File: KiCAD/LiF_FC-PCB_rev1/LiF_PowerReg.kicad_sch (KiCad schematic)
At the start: 32 parts, among them J1 VCH1_{EN}, J2 VCH2_{EN}, J27 R5V0_{EN}, J28 A3V3_{EN}, J29 R3V3_{EN}, J30 REG_{EN}, U10 TLV75533PDBV, U11 TLV75533PDBV, U9 LMR14050

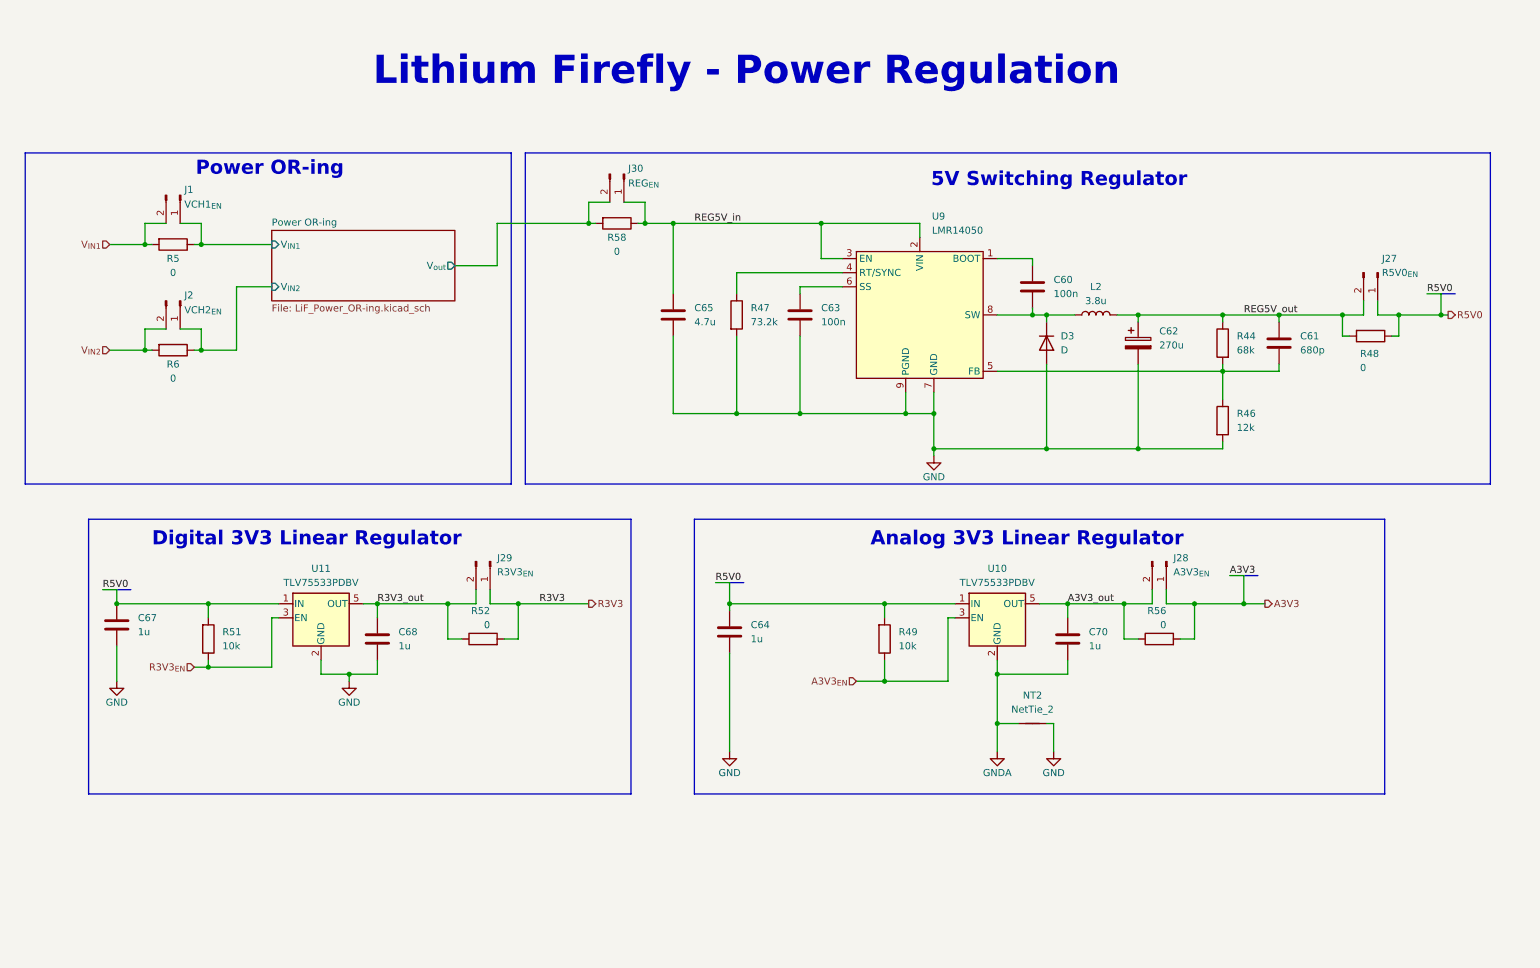
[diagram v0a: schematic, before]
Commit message: changed 5V regulator to support 5V in up to 20V in
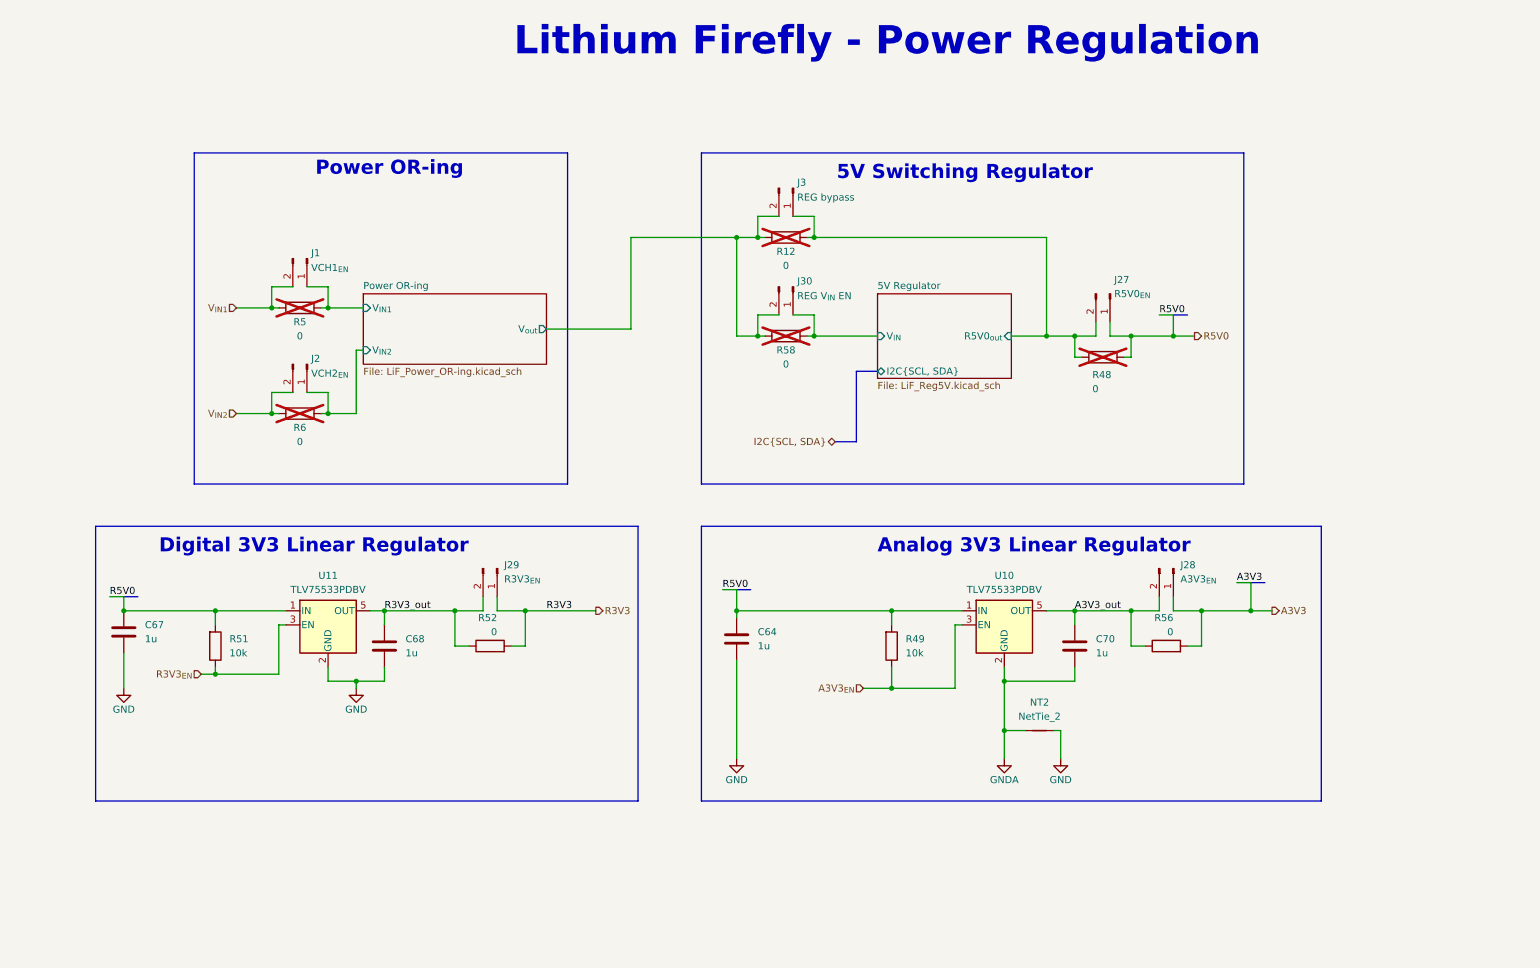
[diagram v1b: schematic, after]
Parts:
- removed C60, C63: 100n, Capacitor_SMD:C_0805_2012Metric, symbol Device:C
- removed C61: 680p, Capacitor_SMD:C_0805_2012Metric, symbol Device:C
- removed C62: 270u, Capacitor_SMD:CP_Elec_6.3x9.9, symbol Device:C_Polarized
- removed C65: 4.7u, Capacitor_SMD:C_0805_2012Metric, symbol Device:C
- removed D3: D, Diode_SMD:D_PowerDI-5, symbol Device:D
- removed L2: 3.8u, MatsLibrary:IND_BOURNS_SRU1038, symbol Device:L
- removed R44: 68k, Resistor_SMD:R_0805_2012Metric, symbol Device:R
- removed R46: 12k, Resistor_SMD:R_0805_2012Metric, symbol Device:R
- removed R47: 73.2k, Resistor_SMD:R_0805_2012Metric, symbol Device:R
- removed U9: LMR14050, Package_SO:Texas_R-PDSO-G8_EP2.95x4.9mm_Mask2.4x3.1mm, symbol MatsKiLibrary:LMR14050SDDAR
- added J3: REG bypass, Connector_PinHeader_1.27mm:PinHeader_1x02_P1.27mm_Vertical, symbol Connector:Conn_01x02_Pin
- added R12: 0, Resistor_SMD:R_0805_2012Metric, symbol Device:R
- J30: value REG_{EN} -> REG V_{IN} EN
- R48, R5, R58, R6: now not fitted
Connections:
- net Power OR-ing/V_{out}: now also J3.2 (Pin_2), R12.2
- net REG5V_in renamed 5V Regulator/V_{IN}
- net REG5V_out renamed 5V Regulator/R5V0_{out}
- net 5V Regulator/R5V0_{out}: now also J3.1 (Pin_1), R12.1
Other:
- added sheet 5V Regulator (LiF_Reg5V.kicad_sch)
- moved on the sheet: C64, C67, C68, C70, J1, J2, J27, J28, J29, J30, NT2, R49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

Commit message: reverted 5V reg, reworked power distribution logic, swapped power OR-ing ICs
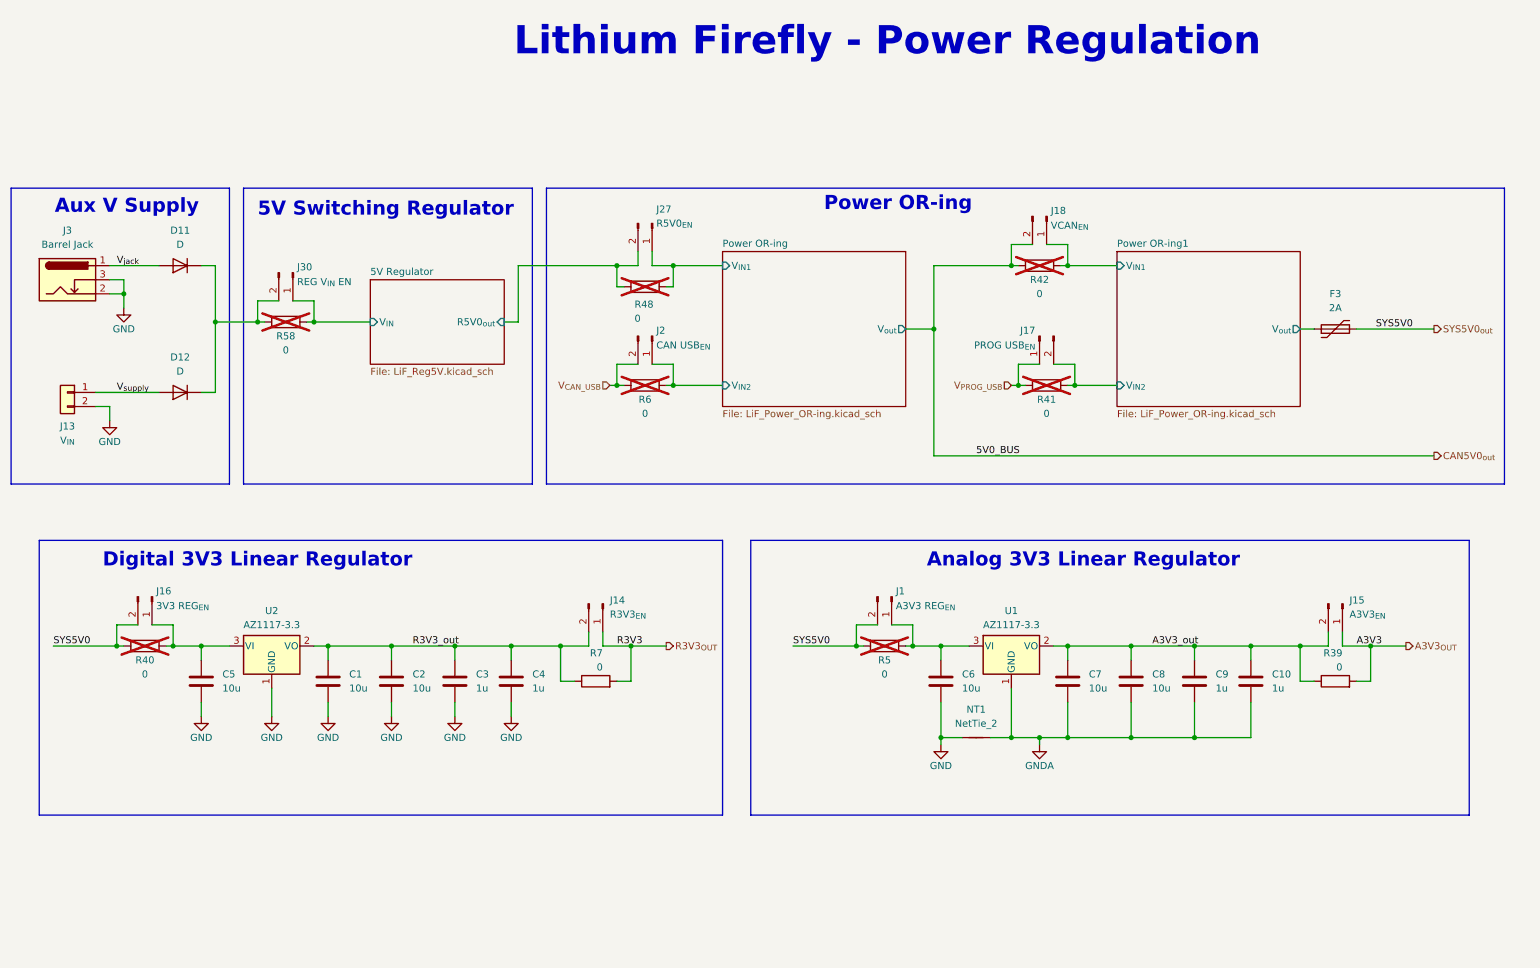
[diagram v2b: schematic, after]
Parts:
- removed C64, C67, C68, C70: 1u, Capacitor_SMD:C_0805_2012Metric, symbol Device:C
- removed J28: A3V3_{EN}, Connector_PinHeader_1.27mm:PinHeader_1x02_P1.27mm_Vertical, symbol Connector:Conn_01x02_Pin
- removed J29: R3V3_{EN}, Connector_PinHeader_1.27mm:PinHeader_1x02_P1.27mm_Vertical, symbol Connector:Conn_01x02_Pin
- removed J3: REG bypass, Connector_PinHeader_1.27mm:PinHeader_1x02_P1.27mm_Vertical, symbol Connector:Conn_01x02_Pin
- removed NT2: NetTie_2, NetTie:NetTie-2_SMD_Pad0.5mm, symbol Device:NetTie_2
- removed R12, R52, R56: 0, Resistor_SMD:R_0805_2012Metric, symbol Device:R
- removed R49, R51: 10k, Resistor_SMD:R_0805_2012Metric, symbol Device:R
- removed U10, U11: TLV75533PDBV, Package_TO_SOT_SMD:SOT-23-5, symbol Regulator_Linear:TLV75533PDBV
- added C1, C2, C5, C6, C7, C8: 10u, Capacitor_SMD:C_0805_2012Metric, symbol Device:C
- added C10, C3, C4, C9: 1u, Capacitor_SMD:C_0805_2012Metric, symbol Device:C
- added D11, D12: D, Diode_SMD:D_SOD-123F, symbol Device:D
- added F3: 2A, symbol Device:Polyfuse
- added J13: V_{IN}, symbol Connector_Generic:Conn_01x02
- added J14: R3V3_{EN}, Connector_PinHeader_1.27mm:PinHeader_1x02_P1.27mm_Vertical, symbol Connector:Conn_01x02_Pin
- added J15: A3V3_{EN}, Connector_PinHeader_1.27mm:PinHeader_1x02_P1.27mm_Vertical, symbol Connector:Conn_01x02_Pin
- added J16: 3V3 REG_{EN}, Connector_PinHeader_1.27mm:PinHeader_1x02_P1.27mm_Vertical, symbol Connector:Conn_01x02_Pin
- added J17: PROG USB_{EN}, Connector_PinHeader_1.27mm:PinHeader_1x02_P1.27mm_Vertical, symbol Connector:Conn_01x02_Pin
- added J18: VCAN_{EN}, Connector_PinHeader_1.27mm:PinHeader_1x02_P1.27mm_Vertical, symbol Connector:Conn_01x02_Pin
- added J3: Barrel Jack, Connector_BarrelJack:BarrelJack_GCT_DCJ200-10-A_Horizontal, symbol Connector:Barrel_Jack_Switch
- added NT1: NetTie_2, NetTie:NetTie-2_SMD_Pad0.5mm, symbol Device:NetTie_2
- added R39, R40, R41, R42, R7: 0, Resistor_SMD:R_0805_2012Metric, symbol Device:R
- added U1, U2: AZ1117-3.3, Package_TO_SOT_SMD:SOT-223-3_TabPin2, symbol Regulator_Linear:AZ1117-3.3
- J1: value VCH1_{EN} -> A3V3 REG_{EN}
- J2: value VCH2_{EN} -> CAN USB_{EN}
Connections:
- net R5V0 is gone; now on net Power OR-ing/V_{IN1}: J27.1 (Pin_1), R48.1
- net A3V3_out: now also C10.1, C7.1, C8.1, C9.1, J15.2 (Pin_2), R39.1, U1.2 (VO)
- net GND: now also C1.2, C2.2, C3.2, C4.2, C5.2, C6.2, J13.2 (Pin_2), J3.2, J3.3, NT1.1, U2.1 (GND)
- net GNDA: now also C10.2, C7.2, C8.2, C9.2, NT1.2, U1.1 (GND)
- net Power OR-ing/V_{IN1}: no longer J1.1 (Pin_1), R5.1
- net R3V3_out: now also C1.1, C2.1, C3.1, C4.1, J14.2 (Pin_2), R7.1, U2.2 (VO)
- net Power OR-ing/V_{out}: no longer names the net of J30.2 (Pin_2), R58.2
- net Power OR-ing/V_{out}: now also D11.1 (K), D12.1 (K)
- net V_{IN1} renamed SYS5V0_{out}
- net SYS5V0_{out}: now also F3.2, J16.2 (Pin_2), R40.2
- net V_{IN2} renamed V_{CAN_USB}
- new net: C5.1, J16.1 (Pin_1), R40.1, U2.3 (VI)
- new net: C6.1, J1.1 (Pin_1), R5.1, U1.3 (VI)
- new net A3V3_{OUT}: J15.1 (Pin_1), R39.2
- new net CAN5V0_{out}: J18.2 (Pin_2), R42.2
- new net Power OR-ing1/V_{IN1}: J18.1 (Pin_1), R42.1
- new net Power OR-ing1/V_{IN2}: J17.2 (Pin_2), R41.1
- new net Power OR-ing1/V_{out}: F3.1
- new net R3V3_{OUT}: J14.1 (Pin_1), R7.2
- new net V_{PROG_USB}: J17.1 (Pin_1), R41.2
- new net V_{jack}: D11.2 (A), J3.1
- new net V_{supply}: D12.2 (A), J13.1 (Pin_1)
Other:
- added sheet Power OR-ing1 (LiF_Power_OR-ing.kicad_sch)
- sheet 5V Regulator ports: added none; removed I2C{SCL, SDA}
- note added: "Aux V Supply"
- moved on the sheet: J2, J27, J30, R48, R58, R6

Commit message: Finished schematics, mostly. Only MCU sheet left. Doing component sourcing
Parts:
- C1: renamed from C5; DKPN (none) -> 490-6473-1-ND; PN (none) -> GRM21BR61C106KE15K
- C10, C9: DKPN (none) -> 490-1691-1-ND; PN (none) -> GRM21BR71C105KA01L
- C2: renamed from C1; DKPN (none) -> 490-6473-1-ND; PN (none) -> GRM21BR61C106KE15K
- C3: renamed from C2; DKPN (none) -> 490-6473-1-ND; PN (none) -> GRM21BR61C106KE15K
- C4: renamed from C3; DKPN (none) -> 490-1691-1-ND; PN (none) -> GRM21BR71C105KA01L
- C5: renamed from C4; DKPN (none) -> 490-1691-1-ND; PN (none) -> GRM21BR71C105KA01L
- C6, C7, C8: DKPN (none) -> 490-6473-1-ND; PN (none) -> GRM21BR61C106KE15K
- F1: renamed from F3; footprint (none) -> Fuse:Fuse_0805_2012Metric; DKPN (none) -> 283-3164-1-ND; PN (none) -> PTS18128V200
- J1: renamed from J18; footprint Connector_PinHeader_1.27mm:PinHeader_1x02_P1.27mm_Vertical -> Connector_PinHeader_2.54mm:PinHeader_1x02_P2.54mm_Vertical
- J10: renamed from J14; footprint Connector_PinHeader_1.27mm:PinHeader_1x02_P1.27mm_Vertical -> Connector_PinHeader_2.54mm:PinHeader_1x02_P2.54mm_Vertical
- J11: renamed from J15; footprint Connector_PinHeader_1.27mm:PinHeader_1x02_P1.27mm_Vertical -> Connector_PinHeader_2.54mm:PinHeader_1x02_P2.54mm_Vertical
- J2: renamed from J27; footprint Connector_PinHeader_1.27mm:PinHeader_1x02_P1.27mm_Vertical -> Connector_PinHeader_2.54mm:PinHeader_1x02_P2.54mm_Vertical
- J3: renamed from J30; footprint Connector_PinHeader_1.27mm:PinHeader_1x02_P1.27mm_Vertical -> Connector_PinHeader_2.54mm:PinHeader_1x02_P2.54mm_Vertical
- J5: renamed from J2; footprint Connector_PinHeader_1.27mm:PinHeader_1x02_P1.27mm_Vertical -> Connector_PinHeader_2.54mm:PinHeader_1x02_P2.54mm_Vertical
- J6: renamed from J17; footprint Connector_PinHeader_1.27mm:PinHeader_1x02_P1.27mm_Vertical -> Connector_PinHeader_2.54mm:PinHeader_1x02_P2.54mm_Vertical
- J7: renamed from J13; footprint (none) -> Connector_JST:JST_PH_B2B-PH-K_1x02_P2.00mm_Vertical
- J8: renamed from J16; footprint Connector_PinHeader_1.27mm:PinHeader_1x02_P1.27mm_Vertical -> Connector_PinHeader_2.54mm:PinHeader_1x02_P2.54mm_Vertical
- J9: renamed from J1; footprint Connector_PinHeader_1.27mm:PinHeader_1x02_P1.27mm_Vertical -> Connector_PinHeader_2.54mm:PinHeader_1x02_P2.54mm_Vertical
- renumbered D11 to D1, D12 to D2, J3 to J4, R42 to R1, R48 to R2, R58 to R3, R6 to R4, R41 to R5, R40 to R6, R5 to R7, R7 to R8, R39 to R9, U2 to U1, U1 to U2
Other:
- company: (none) -> Lithium Firefly Team

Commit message: fixing ERC bugs on schematic. Only MCU left
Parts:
- added TP12, TP13, TP16, TP17: GND, TestPoint:TestPoint_Bridge_Pitch2.54mm_Drill1.0mm, symbol Connector:TestPoint
- added TP14: 5V0 BUS, TestPoint:TestPoint_Bridge_Pitch2.54mm_Drill1.0mm, symbol Connector:TestPoint
- added TP15: SYS 5V0, TestPoint:TestPoint_Bridge_Pitch2.54mm_Drill1.0mm, symbol Connector:TestPoint
- added TP18: V_{AUX}, TestPoint:TestPoint_Bridge_Pitch2.54mm_Drill1.0mm, symbol Connector:TestPoint
- added TP8: R3V3, TestPoint:TestPoint_Bridge_Pitch2.54mm_Drill1.0mm, symbol Connector:TestPoint
- added TP9: A3V3, TestPoint:TestPoint_Bridge_Pitch2.54mm_Drill1.0mm, symbol Connector:TestPoint
- U1, U2: DKPN (none) -> AZ1117CH-3.3TRG1DICT-ND; PN (none) -> AZ1117CH-3.3TRG1
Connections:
- net 5V Regulator/V_{IN}: now also TP18.1
- net A3V3_out: now also TP9.1
- net CAN5V0_{out}: now also TP14.1
- net GND: now also TP12.1, TP13.1, TP16.1, TP17.1
- net R3V3_out: now also TP8.1
- net SYS5V0_{out}: now also TP15.1
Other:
- sheet Power OR-ing ports: added Status; removed none
- sheet Power OR-ing1 ports: added Status; removed none
